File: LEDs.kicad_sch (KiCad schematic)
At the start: 6 parts

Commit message: layout kinda screwy but it works?
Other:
- note added: "PWR: Illuminated when 12V power is present, regardless of source CTRLS: Illuminated when controls (IN2) source is selected EXT: Illuminated when external (IN1) source is selected"
- note removed: "PWR: Illuminated when 12V power is present, regardless of source CTRLS: Illuminated when controls (IN2) source is selected EXT: Illuminated when external(IN1) source is selected"
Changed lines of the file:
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@@
 		)
 	)
-	(text "PWR: Illuminated when 12V\npower is present,\nregardless of source\n\nCTRLS: Illuminated when\ncontrols (IN2) source\nis selected\n\nEXT: Illuminated when\nexternal(IN1) source\nis selected"
+	(text "PWR: Illuminated when 12V\npower is present,\nregardless of source\n\nCTRLS: Illuminated when\ncontrols (IN2) source\nis selected\n\nEXT: Illuminated when\nexternal (IN1) source\nis selected"
 		(exclude_from_sim no)
 		(at 20.574 44.196 0)

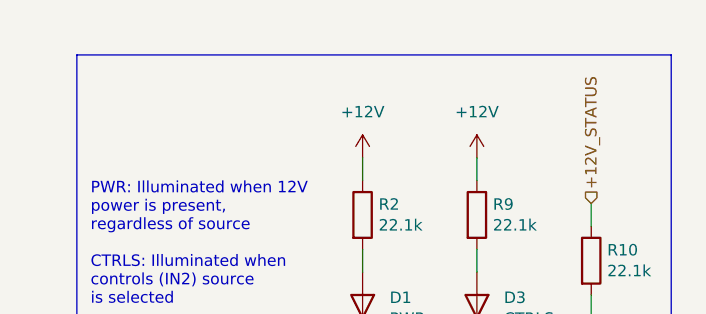
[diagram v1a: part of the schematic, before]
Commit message: add reverse polarity for both inputs, fixed muxing logic i think
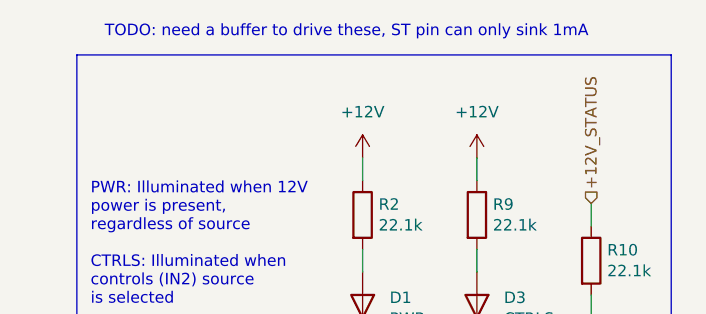
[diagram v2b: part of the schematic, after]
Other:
- note added: "TODO: need a buffer to drive these, ST pin can only sink 1mA"
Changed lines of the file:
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@@
+		)
+	)
+	(text "TODO: need a buffer to drive these, ST pin can only sink 1mA"
+		(exclude_from_sim no)
+		(at 49.022 16.51 0)
+		(effects
+			(font
+				(size 1.27 1.27)
+			)
 		)
 	)

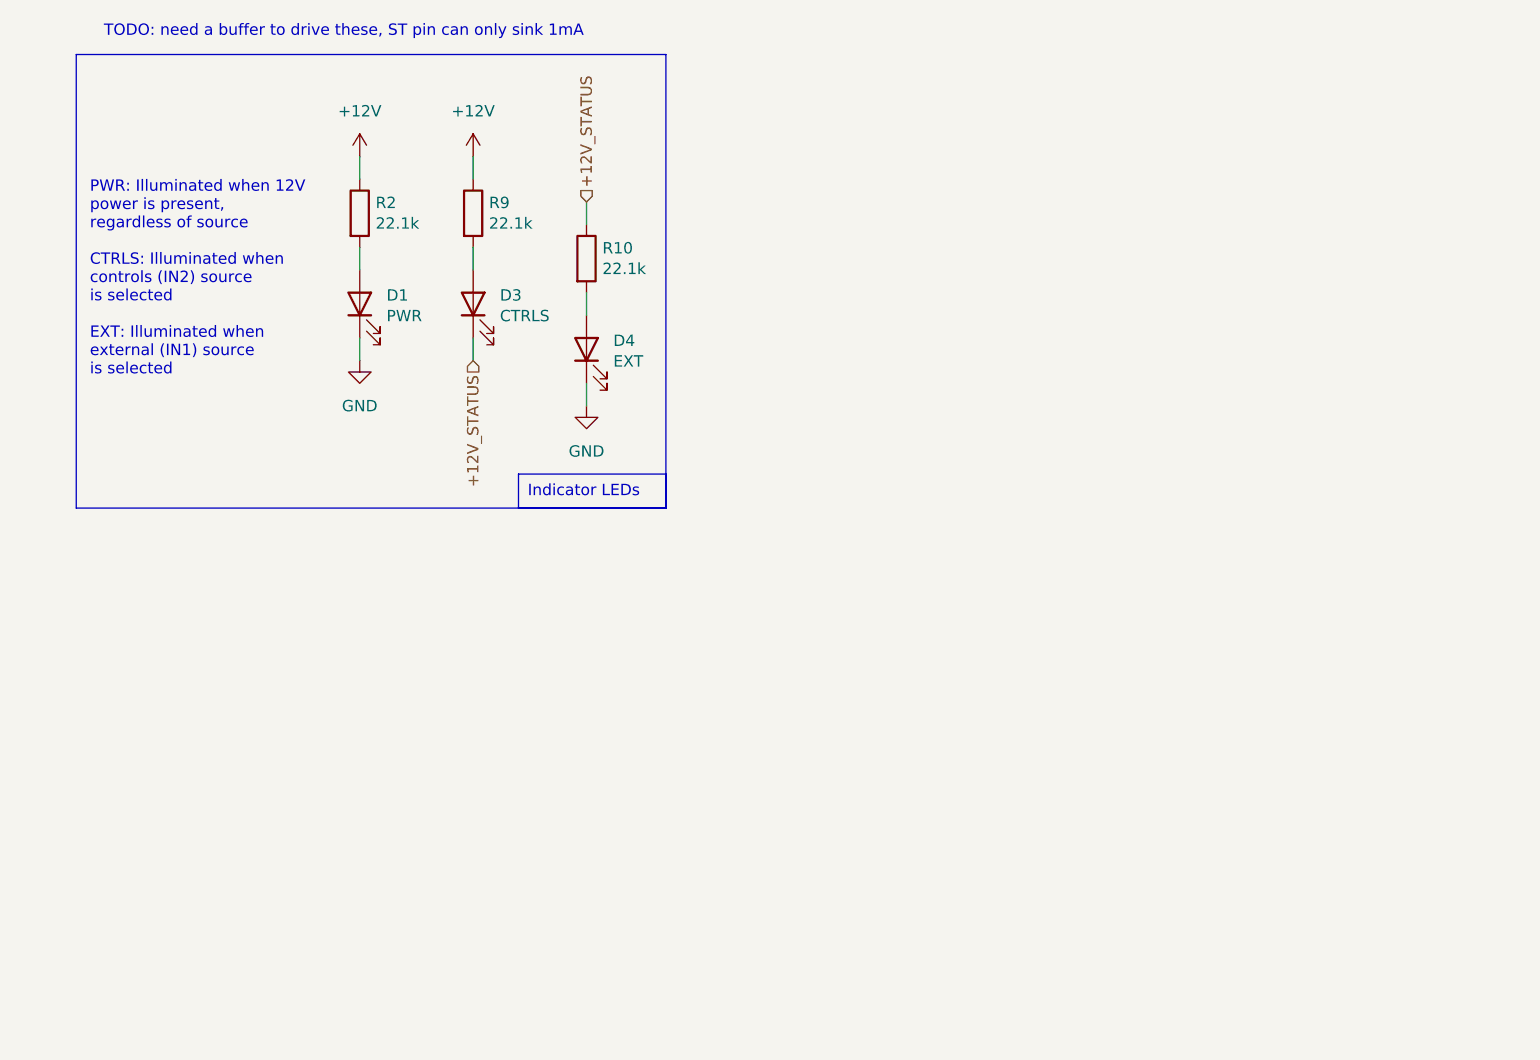
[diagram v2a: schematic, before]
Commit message: symbol/footprint for RUM001L02T2CL
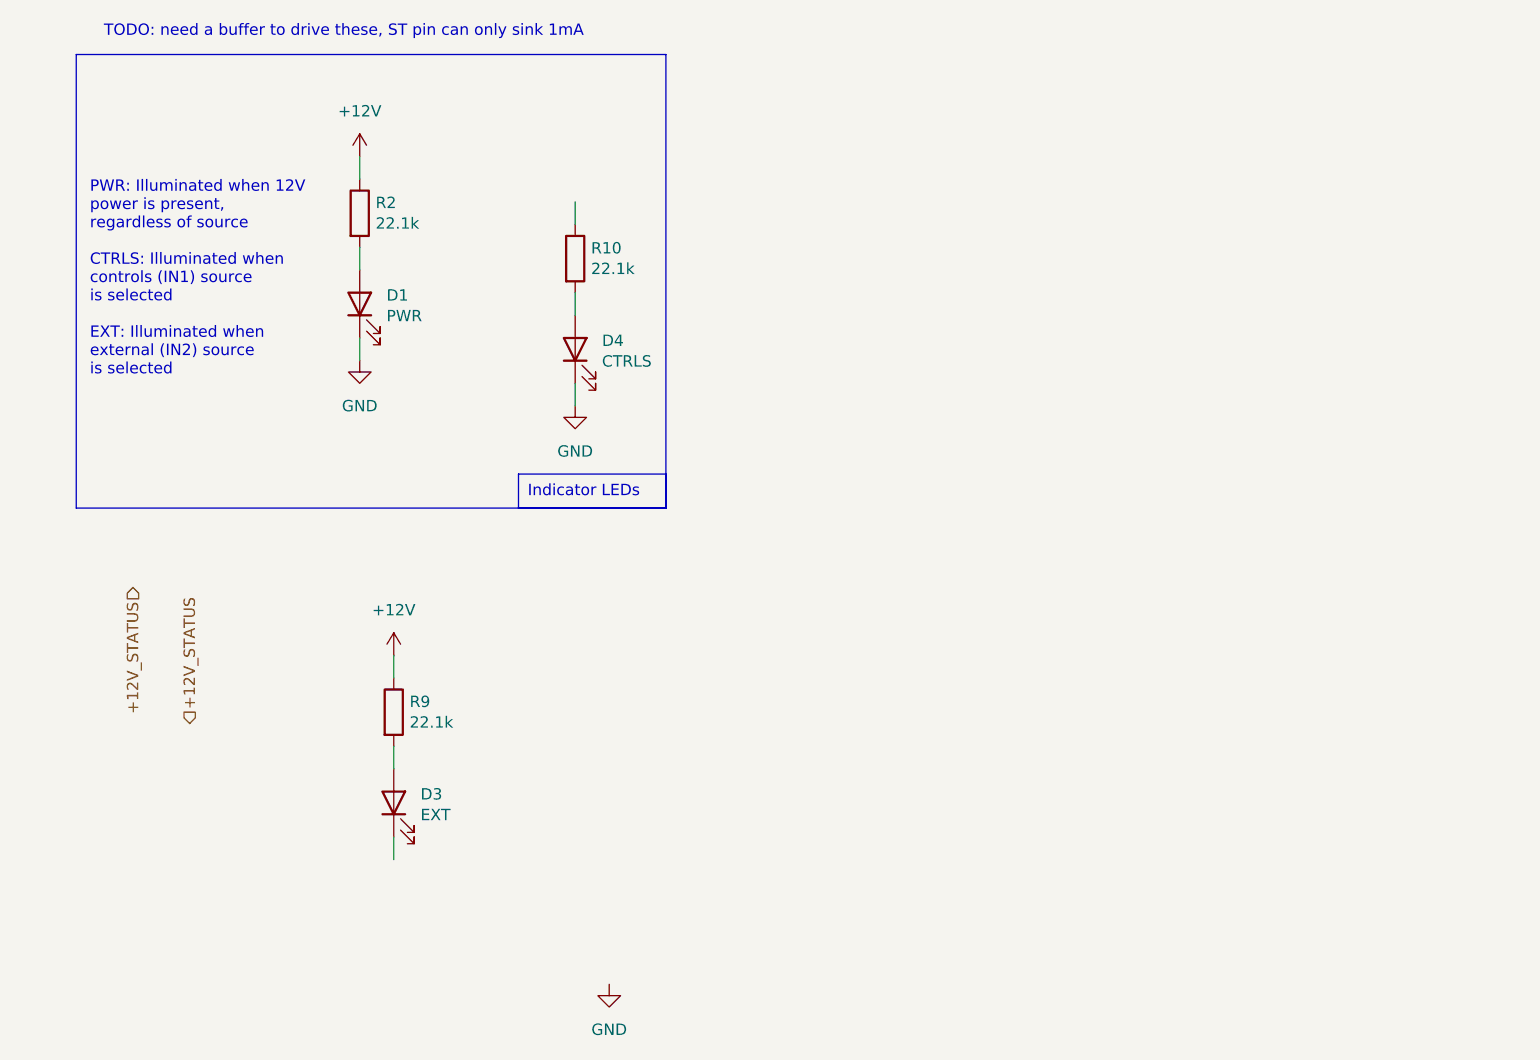
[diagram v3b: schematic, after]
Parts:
- D3: value CTRLS -> EXT
- D4: value EXT -> CTRLS
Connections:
- net +12V_STATUS: no longer D3.1 (K), R10.1
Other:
- note added: "PWR: Illuminated when 12V power is present, regardless of source CTRLS: Illuminated when controls (IN1) source is selected EXT: Illuminated when external (IN2) source is selected"
- note removed: "PWR: Illuminated when 12V power is present, regardless of source CTRLS: Illuminated when controls (IN2) source is selected EXT: Illuminated when external (IN1) source is selected"
- moved on the sheet: D3, D4, R10, R9

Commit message: LEDs with mosfet
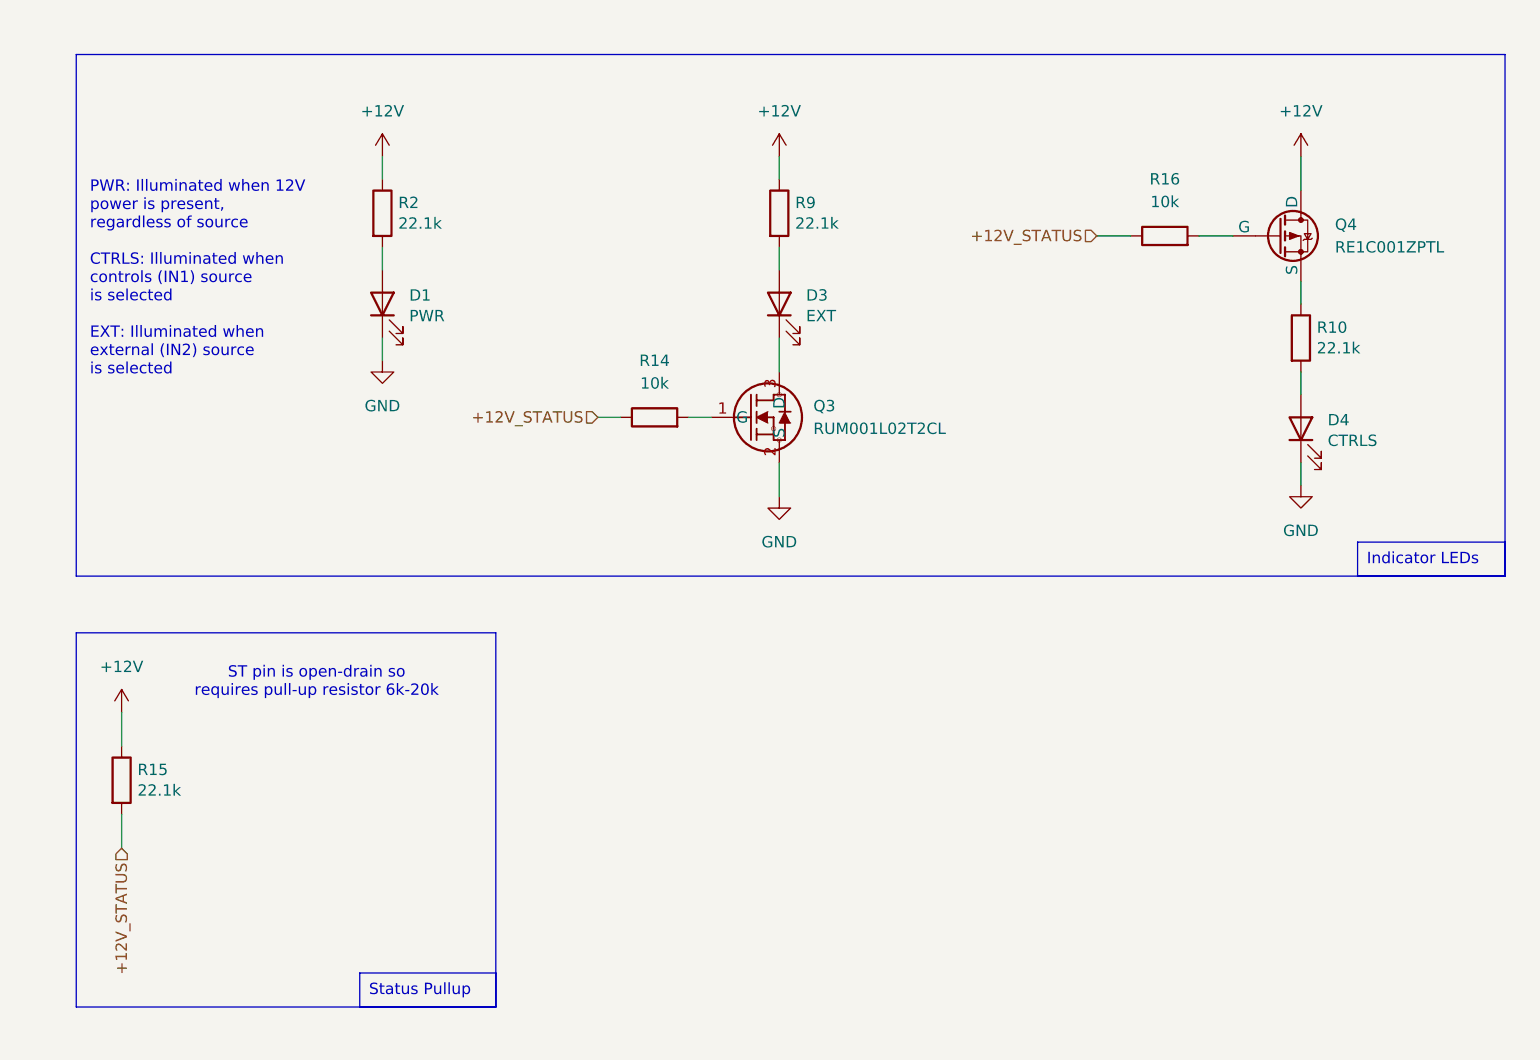
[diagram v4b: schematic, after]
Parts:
- added Q3: RUM001L02T2CL, TRANS_RUM001_ROM, symbol RUM001L02T2CL:RUM001L02T2CL
- added Q4: RE1C001ZPTL, symbol Simulation_SPICE:PMOS
- added R14, R16: 10k, symbol Device:R
- added R15: 22.1k, Resistor_SMD:R_0805_2012Metric, symbol Device:R
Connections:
- net +12V: now also Q4.1 (D), R15.1
- net +12V_STATUS: now also R14.1, R15.2, R16.1
- net GND: now also Q3.2 (S)
- net at D3.1 (K): now also Q3.3 (D)
- net at R10.1: now also Q4.3 (S)
- new net: Q3.1 (G), R14.2
- new net: Q4.2 (G), R16.2
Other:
- note added: "ST pin is open-drain so requires pull-up resistor 6k-20k"
- note removed: "TODO: need a buffer to drive these, ST pin can only sink 1mA"
- moved on the sheet: D1, D3, R2, R9

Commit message: flip connectors so clip faces inside
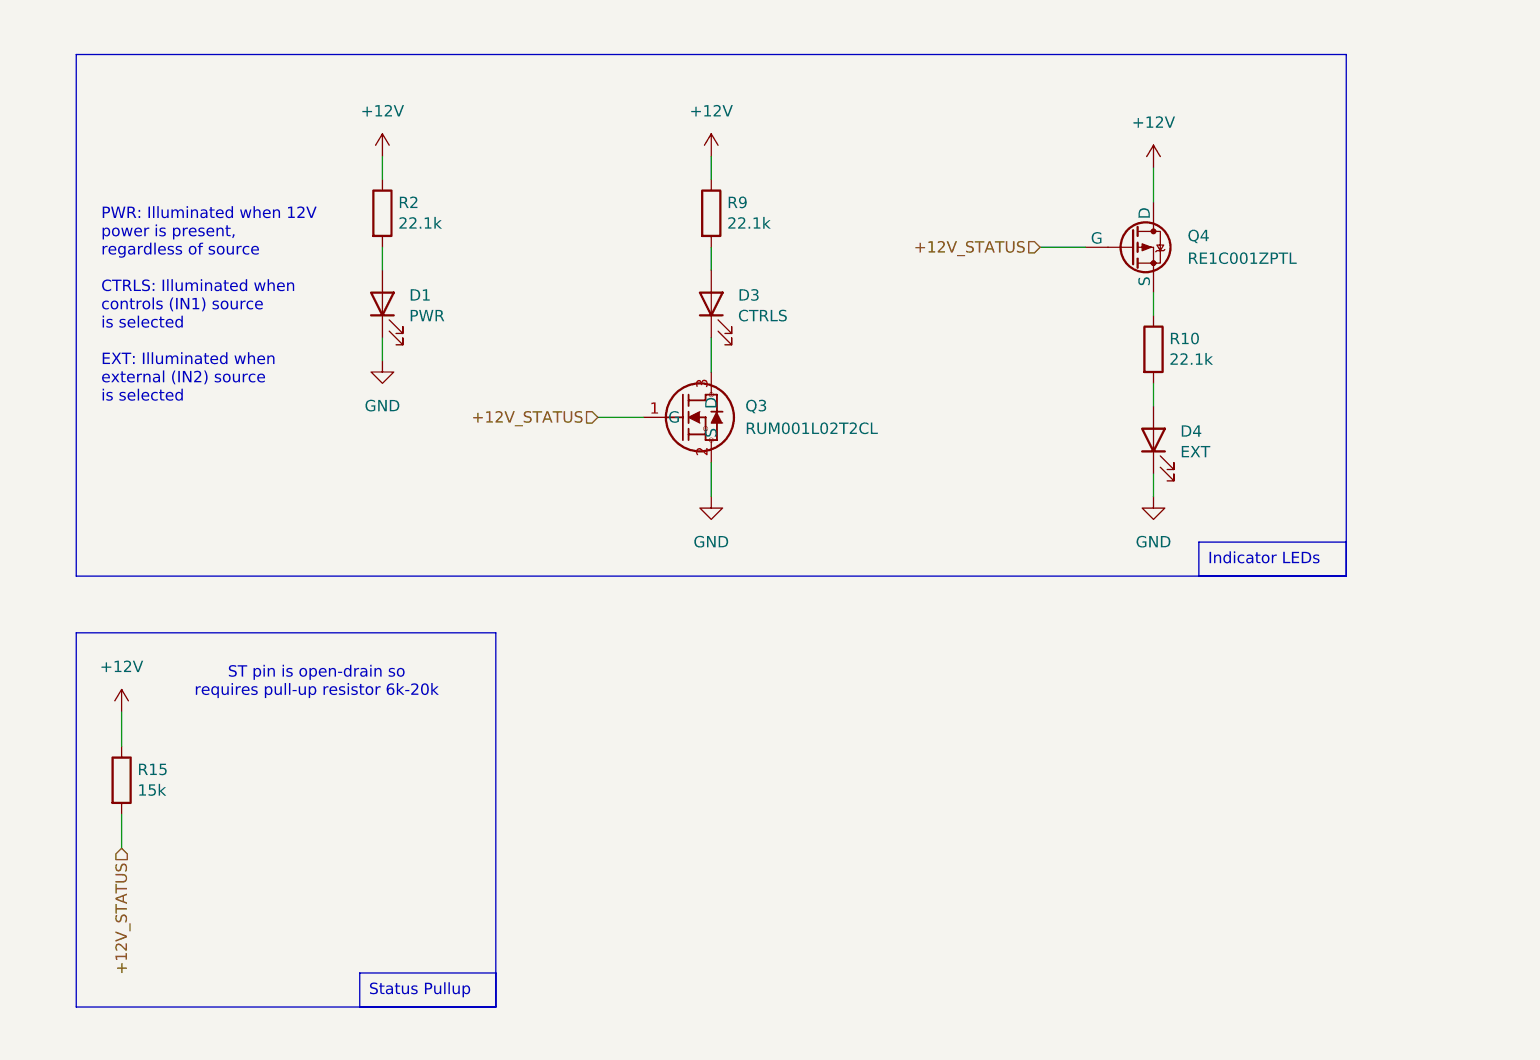
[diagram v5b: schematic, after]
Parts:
- removed R14, R16: 10k, symbol Device:R
- D3: value EXT -> CTRLS
- D4: value CTRLS -> EXT
- Q3: footprint TRANS_RUM001_ROM -> RUM001L02T2CL:TRANS_RUM001_ROM
- Q4: footprint (none) -> RE1C001ZPTL:TRANS_RE1C001_ROM
- R15: value 22.1k -> 15k
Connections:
- net +12V_STATUS: now also Q3.1 (G), Q4.2 (G)
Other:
- moved on the sheet: D3, D4, Q3, Q4, R10, R9
